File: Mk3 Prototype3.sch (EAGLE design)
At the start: 151 parts, among them IC1 TPD3E001DRL, IC2 TPS62082, IC3 STM32F401V, IC4 BQ24092, IC6 CC3100MOD, IC7 BQ2970, IC8 LSM6DS3, IC9 LIS3MDL, J1 ZX62-AB-5PA(11), J2 ER-CON50HT-1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

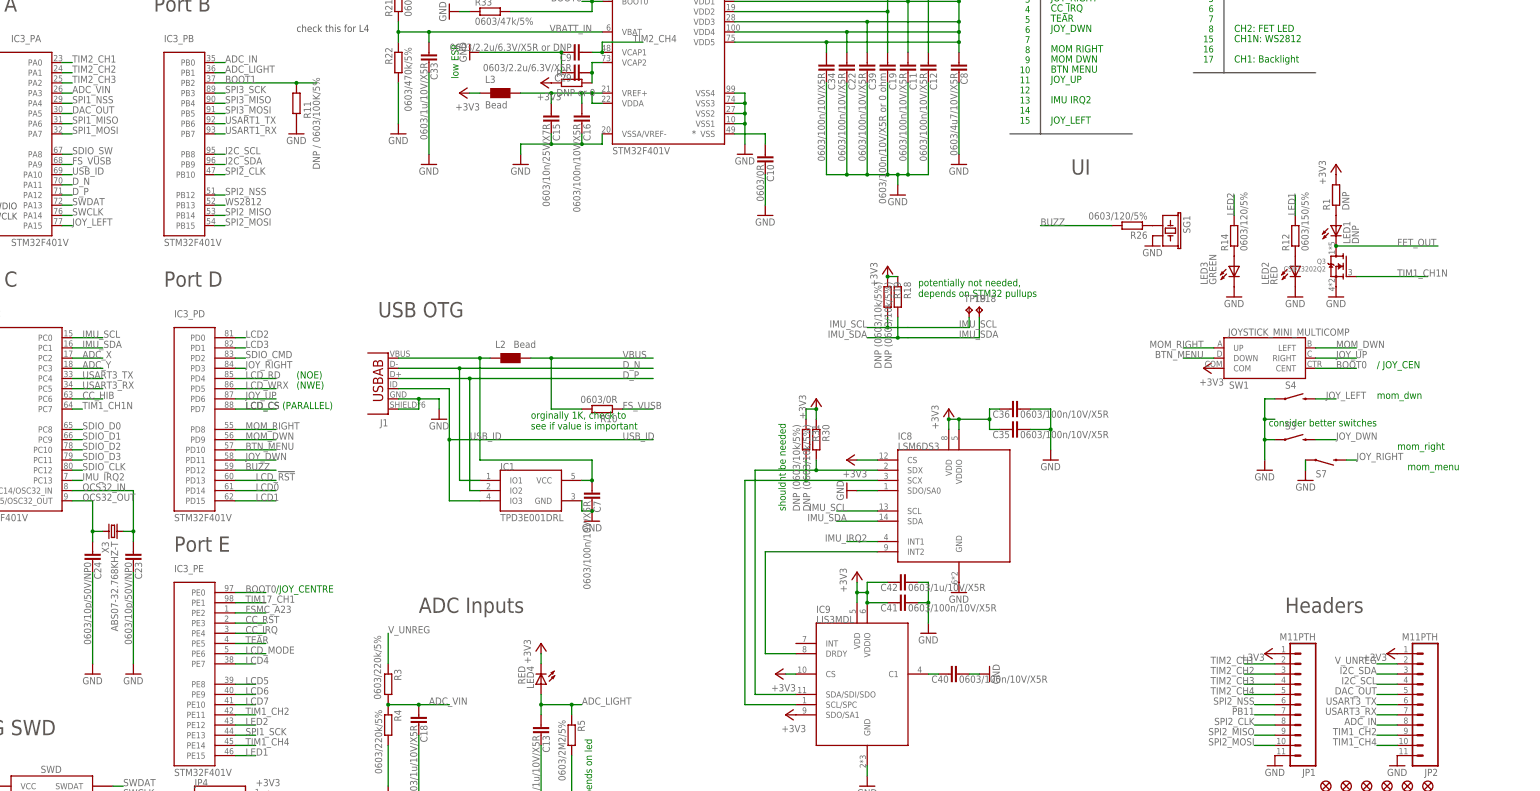
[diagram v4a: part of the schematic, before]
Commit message: all gpio now connected
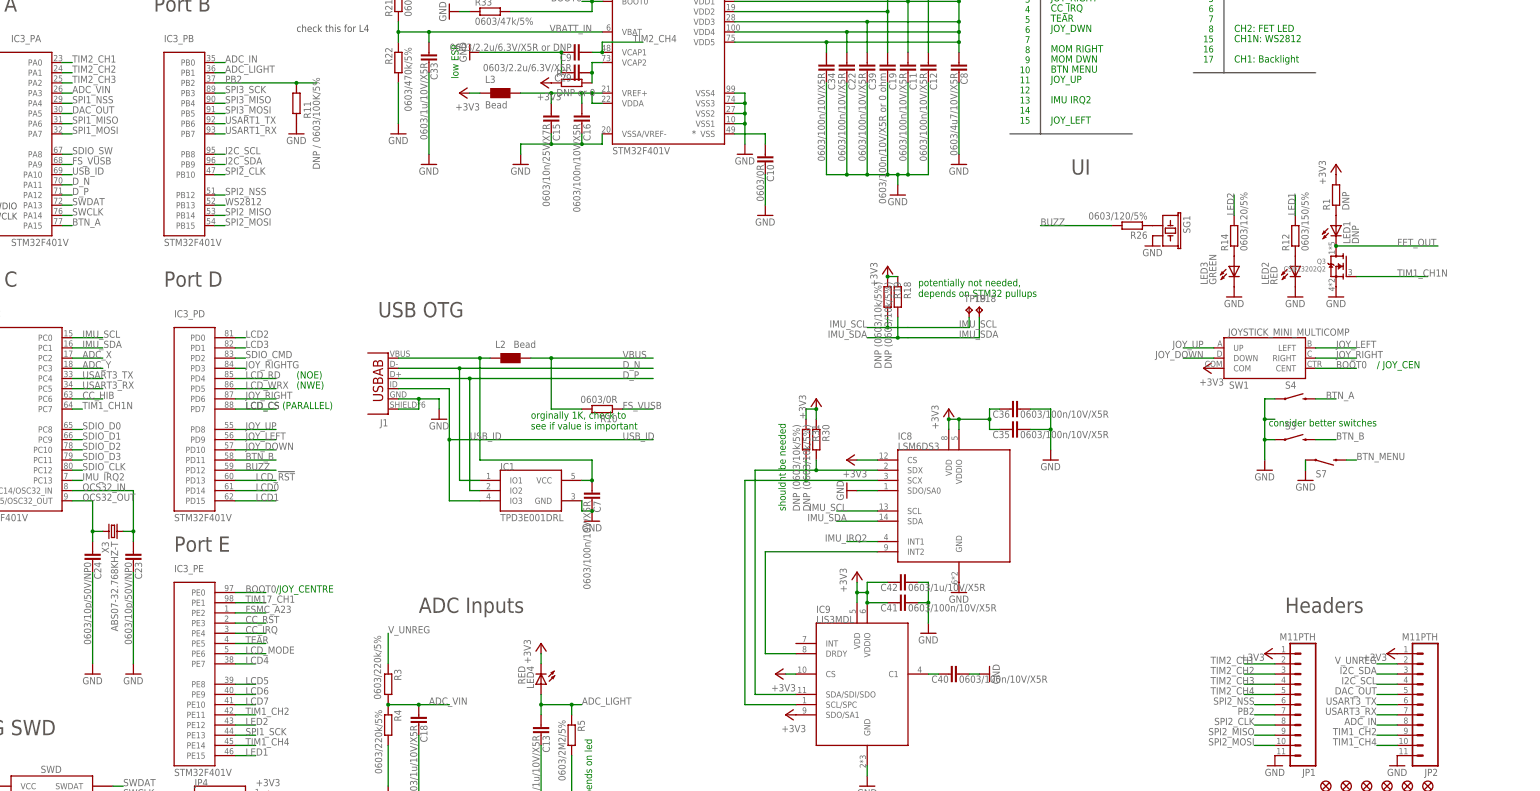
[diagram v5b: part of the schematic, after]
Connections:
- net JOY_DWN renamed BTN_B
- removed net BOOT1: IC3_PB.PB2, R11.2
- removed net MOM_DWN: IC3_PD.PD9, SW1.LEFT
- removed net MOM_RIGHT: IC3_PD.PD8, SW1.UP
- removed net PB11: JP1.7
- new net BTN_A: IC3_PA.PA15, S4.2
- new net JOY_DOWN: IC3_PD.PD10, SW1.DOWN
- new net JOY_RIGHTG: IC3_PD.PD3
- new net PB2: IC3_PB.PB2, JP1.7, R11.2
- net BTN_MENU: now also S7.2; no longer IC3_PD.PD10, SW1.DOWN
- net JOY_LEFT: now also IC3_PD.PD9, SW1.LEFT; no longer IC3_PA.PA15, S4.2
- net JOY_RIGHT: now also IC3_PD.PD6, SW1.RIGHT; no longer IC3_PD.PD3, S7.2
- net JOY_UP: now also IC3_PD.PD8, SW1.UP; no longer IC3_PD.PD6, SW1.RIGHT
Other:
- note removed: "mom_dwn"
- note removed: "mom_menu"
- note removed: "mom_right"
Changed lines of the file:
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@@
 <wire x1="259.08" y1="246.38" x2="246.38" y2="246.38" width="0.1524" layer="97"/>
 <wire x1="246.38" y1="243.84" x2="259.08" y2="243.84" width="0.1524" layer="97"/>
-<text x="358.14" y="119.38" size="1.778" layer="91">mom_dwn</text>
-<text x="363.22" y="106.68" size="1.778" layer="91">mom_right</text>
-<text x="365.76" y="101.6" size="1.778" layer="91">mom_menu</text>
 <text x="314.96" y="246.38" size="3.81" layer="97" ratio="15">Timers List</text>
 <text x="317.5" y="203.2" size="1.6764" layer="91" ratio="11" align="bottom-right">1
@@
 </segment>
 </net>
-<net name="PB11" class="0">
+<net name="PB2" class="0">
 <segment>
 <wire x1="332.74" y1="40.64" x2="327.66" y2="40.64" width="0.1524" layer="91"/>
@@
 <pinref part="JP1" gate="G$1" pin="7"/>
 </segment>
+<segment>
+<pinref part="IC3" gate="_PB" pin="PB2"/>
+<label x="71.12" y="198.12" size="1.778" layer="95"/>
+<pinref part="R11" gate="G$1" pin="2"/>
+<wire x1="68.58" y1="198.12" x2="88.9" y2="198.12" width="0.1524" layer="91"/>
+<junction x="88.9" y="198.12"/>
+<wire x1="88.9" y1="198.12" x2="93.98" y2="198.12" width="0.1524" layer="91"/>
+</segment>
 </net>
 <net name="VBATT_IN" class="0">
@@
 </segment>
 </net>
-<net name="JOY_UP" class="0">
+<net name="JOY_RIGHT" class="0">
 <segment>
 <pinref part="IC3" gate="_PD" pin="PD6"/>
@@
 </segment>
 </net>
-<net name="JOY_DWN" class="0">
+<net name="BTN_B" class="0">
 <segment>
 <pinref part="IC3" gate="_PD" pin="PD11"/>
@@
 </segment>
 </net>
-<net name="JOY_LEFT" class="0">
+<net name="BTN_A" class="0">
 <segment>
 <wire x1="33.02" y1="162.56" x2="30.48" y2="162.56" width="0.1524" layer="91"/>
@@
 </segment>
 </net>
-<net name="JOY_RIGHT" class="0">
+<net name="JOY_RIGHTG" class="0">
 <segment>
 <pinref part="IC3" gate="_PD" pin="PD3"/>
@@
 <label x="76.2" y="127" size="1.778" layer="95"/>
 </segment>
-<segment>
-<pinref part="S7" gate="G$1" pin="2"/>
-<wire x1="350.52" y1="104.14" x2="353.06" y2="104.14" width="0.1524" layer="91"/>
-<label x="353.06" y="104.14" size="1.778" layer="95"/>
-</segment>
 </net>
 <net name="ADC_VIN" class="0">
@@
 </segment>
 </net>
-<net name="MOM_RIGHT" class="0">
+<net name="JOY_UP" class="0">
 <segment>
 <pinref part="IC3" gate="_PD" pin="PD8"/>
@@
 </segment>
 </net>
-<net name="MOM_DWN" class="0">
+<net name="JOY_LEFT" class="0">
 <segment>
 <pinref part="IC3" gate="_PD" pin="PD9"/>
@@
 </segment>
 </net>
-<net name="BTN_MENU" class="0">
+<net name="JOY_DOWN" class="0">
 <segment>
 <pinref part="IC3" gate="_PD" pin="PD10"/>
@@
 </segment>
 </net>
-<net name="BOOT1" class="0">
-<segment>
-<pinref part="IC3" gate="_PB" pin="PB2"/>
-<label x="71.12" y="198.12" size="1.778" layer="95"/>
-<pinref part="R11" gate="G$1" pin="2"/>
-<wire x1="68.58" y1="198.12" x2="88.9" y2="198.12" width="0.1524" layer="91"/>
-<junction x="88.9" y="198.12"/>
-<wire x1="88.9" y1="198.12" x2="93.98" y2="198.12" width="0.1524" layer="91"/>
-</segment>
-</net>
 <net name="ADC_Y" class="0">
 <segment>
@@
 </segment>
 </net>
+<net name="BTN_MENU" class="0">
+<segment>
+<pinref part="S7" gate="G$1" pin="2"/>
+<wire x1="350.52" y1="104.14" x2="353.06" y2="104.14" width="0.1524" layer="91"/>
+<label x="353.06" y="104.14" size="1.778" layer="95"/>
+</segment>
+</net>

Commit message: routing intensifies...
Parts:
- removed SJ2: JUMPER-PAD-3-2OF3_NC_BY_TRACE_SMALL, SparkFun-Passives:JUMPER-PAD-3-2OF3_NC_BY_TRACE_SMALL
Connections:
- removed net JOY_RIGHTG: IC3_PD.PD3
- net +3V3: no longer SJ2.1
- net BTN_MENU: now also IC3_PD.PD3
- net GND: no longer SJ2.3
- net LCD_MODE: no longer SJ2.2
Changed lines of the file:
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@@
 <?xml version="1.0" encoding="utf-8"?>
 <!DOCTYPE eagle SYSTEM "eagle.dtd">
-<eagle version="6.6.0">
+<eagle version="6.5.0">
 <drawing>
 <settings>
@@
 <part name="R32" library="TiLDA Mk3 Parts" deviceset="R-EU_" device="0603K-SMALL" value="DNP (0)"/>
 <part name="GND1" library="TiLDA Mk3 Parts" deviceset="GND" device=""/>
-<part name="SJ2" library="SparkFun-Passives" deviceset="JUMPER-PAD-3-2OF3_NC_BY_TRACE" device="_SMALL"/>
-<part name="GND3" library="TiLDA Mk3 Parts" deviceset="GND" device=""/>
-<part name="+3V9" library="supply1" deviceset="+3V3" device=""/>
 <part name="TP1" library="TiLDA Mk3 Parts" deviceset="TP" device="B1,27"/>
 <part name="TP2" library="TiLDA Mk3 Parts" deviceset="TP" device="B1,27"/>
@@
 <instance part="R32" gate="G$1" x="662.94" y="27.94" rot="R90"/>
 <instance part="GND1" gate="1" x="662.94" y="20.32"/>
-<instance part="SJ2" gate="G$1" x="726.44" y="223.52" rot="MR0"/>
-<instance part="GND3" gate="1" x="726.44" y="215.9"/>
-<instance part="+3V9" gate="G$1" x="726.44" y="231.14"/>
 <instance part="TP1" gate="G$1" x="736.6" y="157.48" smashed="yes">
 <attribute name="NAME" x="735.33" y="158.75" size="1.778" layer="95"/>
@@
 </segment>
 <segment>
-<pinref part="SJ2" gate="G$1" pin="3"/>
-<pinref part="GND3" gate="1" pin="GND"/>
-</segment>
-<segment>
 <pinref part="S1" gate="G$1" pin="2"/>
 <pinref part="GND15" gate="1" pin="GND"/>
@@
 <pinref part="+3V21" gate="G$1" pin="+3V3"/>
 </segment>
-<segment>
-<pinref part="SJ2" gate="G$1" pin="1"/>
-<pinref part="+3V9" gate="G$1" pin="+3V3"/>
-</segment>
 </net>
 <net name="PB2" class="0">
@@
 </segment>
 </net>
-<net name="JOY_RIGHTG" class="0">
-<segment>
-<pinref part="IC3" gate="_PD" pin="PD3"/>
-<wire x1="73.66" y1="127" x2="76.2" y2="127" width="0.1524" layer="91"/>
-<label x="76.2" y="127" size="1.778" layer="95"/>
-</segment>
-</net>
 <net name="ADC_VIN" class="0">
 <segment>
@@
 <pinref part="J2" gate="G$1" pin="IM3"/>
 <label x="726.44" y="223.52" size="1.778" layer="95"/>
-<pinref part="SJ2" gate="G$1" pin="2"/>
 </segment>
 <segment>
@@
 <label x="353.06" y="104.14" size="1.778" layer="95"/>
 </segment>
+<segment>
+<pinref part="IC3" gate="_PD" pin="PD3"/>
+<wire x1="73.66" y1="127" x2="76.2" y2="127" width="0.1524" layer="91"/>
+<label x="76.2" y="127" size="1.778" layer="95"/>
+</segment>
 </net>
